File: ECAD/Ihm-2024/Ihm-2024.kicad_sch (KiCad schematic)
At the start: 15 parts, among them SW1 SW_SPDT, SW2 SW_SPDT, SW3 SW_SPDT, SW4 SW_SPDT

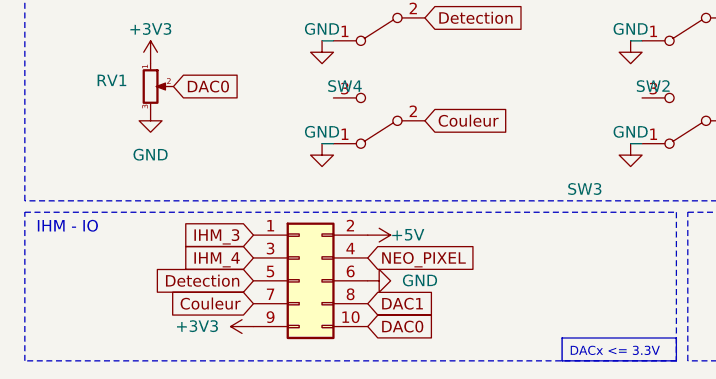
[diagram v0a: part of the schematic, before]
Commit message: update ICD connector
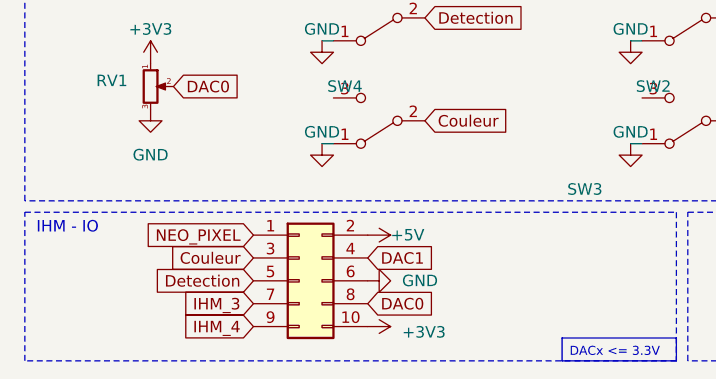
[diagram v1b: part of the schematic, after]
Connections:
- net +3V3: now also IHM-IO1.10 (Pin_10); no longer IHM-IO1.9 (Pin_9)
- net Couleur: now also IHM-IO1.3 (Pin_3); no longer IHM-IO1.7 (Pin_7)
- net DAC0: now also IHM-IO1.8 (Pin_8); no longer IHM-IO1.10 (Pin_10)
- net DAC1: now also IHM-IO1.4 (Pin_4); no longer IHM-IO1.8 (Pin_8)
- net IHM_3: now also IHM-IO1.7 (Pin_7); no longer IHM-IO1.1 (Pin_1)
- net IHM_4: now also IHM-IO1.9 (Pin_9); no longer IHM-IO1.3 (Pin_3)
- net NEO_PIXEL: now also IHM-IO1.1 (Pin_1); no longer IHM-IO1.4 (Pin_4)

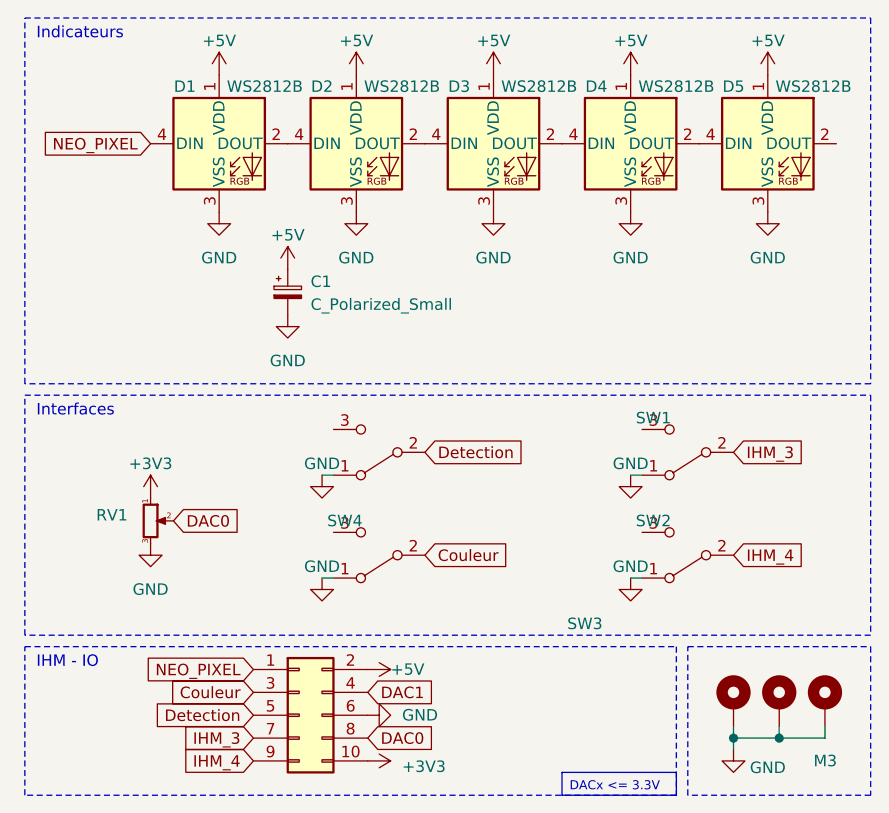
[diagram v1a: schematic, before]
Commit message: add capacitor
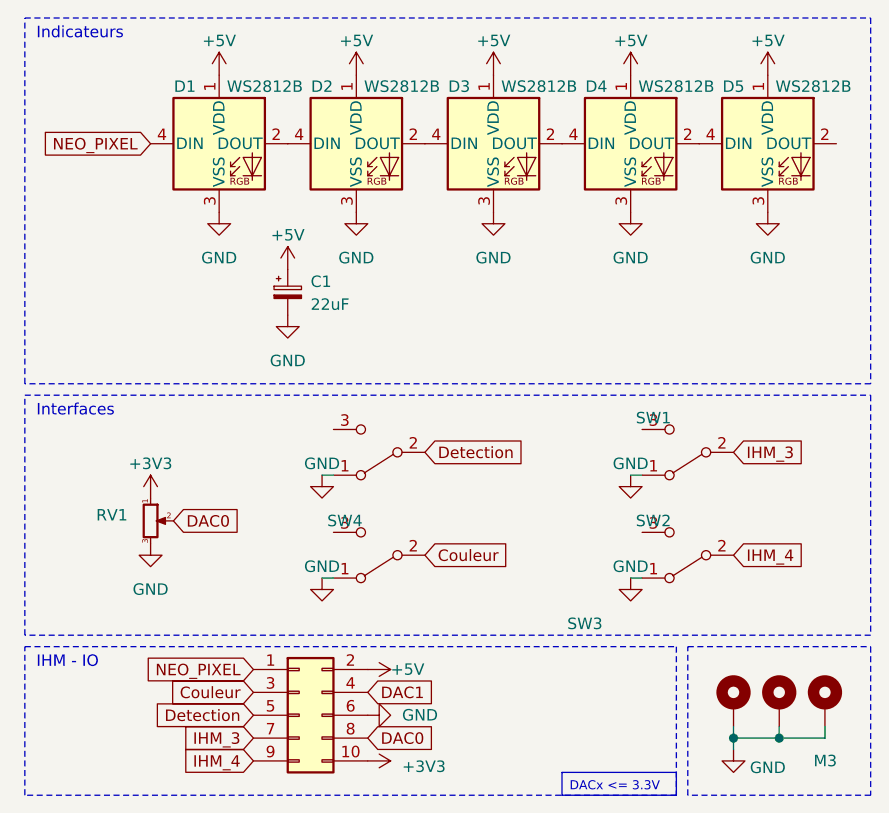
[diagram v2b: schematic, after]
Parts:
- C1: value C_Polarized_Small -> 22uF; footprint (none) -> Capacitor_SMD:CP_Elec_5x5.4
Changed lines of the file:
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@@
       (effects (font (size 1.27 1.27)) (justify left))
     )
-    (property "Value" "C_Polarized_Small" (at 128.27 77.5589 0)
+    (property "Value" "22uF" (at 128.27 77.5589 0)
       (effects (font (size 1.27 1.27)) (justify left))
     )
-    (property "Footprint" "" (at 125.73 76.2 0)
+    (property "Footprint" "Capacitor_SMD:CP_Elec_5x5.4" (at 125.73 76.2 0)
       (effects (font (size 1.27 1.27)) hide)
     )
